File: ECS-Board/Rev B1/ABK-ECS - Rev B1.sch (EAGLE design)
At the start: 295 parts, among them J1 USB-B-S-RA, J10 22-05-7028-02, J11 RB1-125BAG1A, J12 22-05-7068-06, J13 22-05-7048-04, J14 22-05-7048-04, J15 22-05-7048-04, J2 MSTBA2, J3 22-05-7068-06, J4 22-05-7068-06, J5 22-05-7068-06, J6 22-05-7068-06, J7 22-05-7028-02, J8 FTSH-103-01-L-DV-NOPASTE, J9 FTSH-105-01-L-DV-NOPASTE, SW1 B3FS-1015, SW2 B3FS-1015, T1 MMBT2907ALT3, T10 MMBT2222AL, T11 IRLML5103TRPBF, T12 MMBT2222AL, T13 IRLML5103TRPBF, T14 IRLML5103TRPBF, T15 IRLML5103TRPBF, T16 IRLML5103TRPBF, T17 MMBT2222AL, T18 MMBT2222AL, T19 MMBT2222AL, T2 EXMACHINA-LOGO-NAME, T20 MMBT2222AL, T3 IRLML5103TRPBF, T4 IRLML5103TRPBF, T5 IRLML5103TRPBF, T6 IRLML5103TRPBF, T7 MMBT2222AL, T8 MMBT2222AL, T9 MMBT2222AL, U1 AT24C512C-SSHM-B, U2 LPC1768FBD100, U3 LT3686HDDPBF, U4 LT3686HDDPBF, U5 CD4050BD, U6 CD4050BD, U7 DP83848JSQ/NOPB, U8 SN74LVC2G17DBVR, U9 SN74LVC2G17DBVR, X1 FC-135, X2 ASE-12, X3 3000, X4 ASE_50

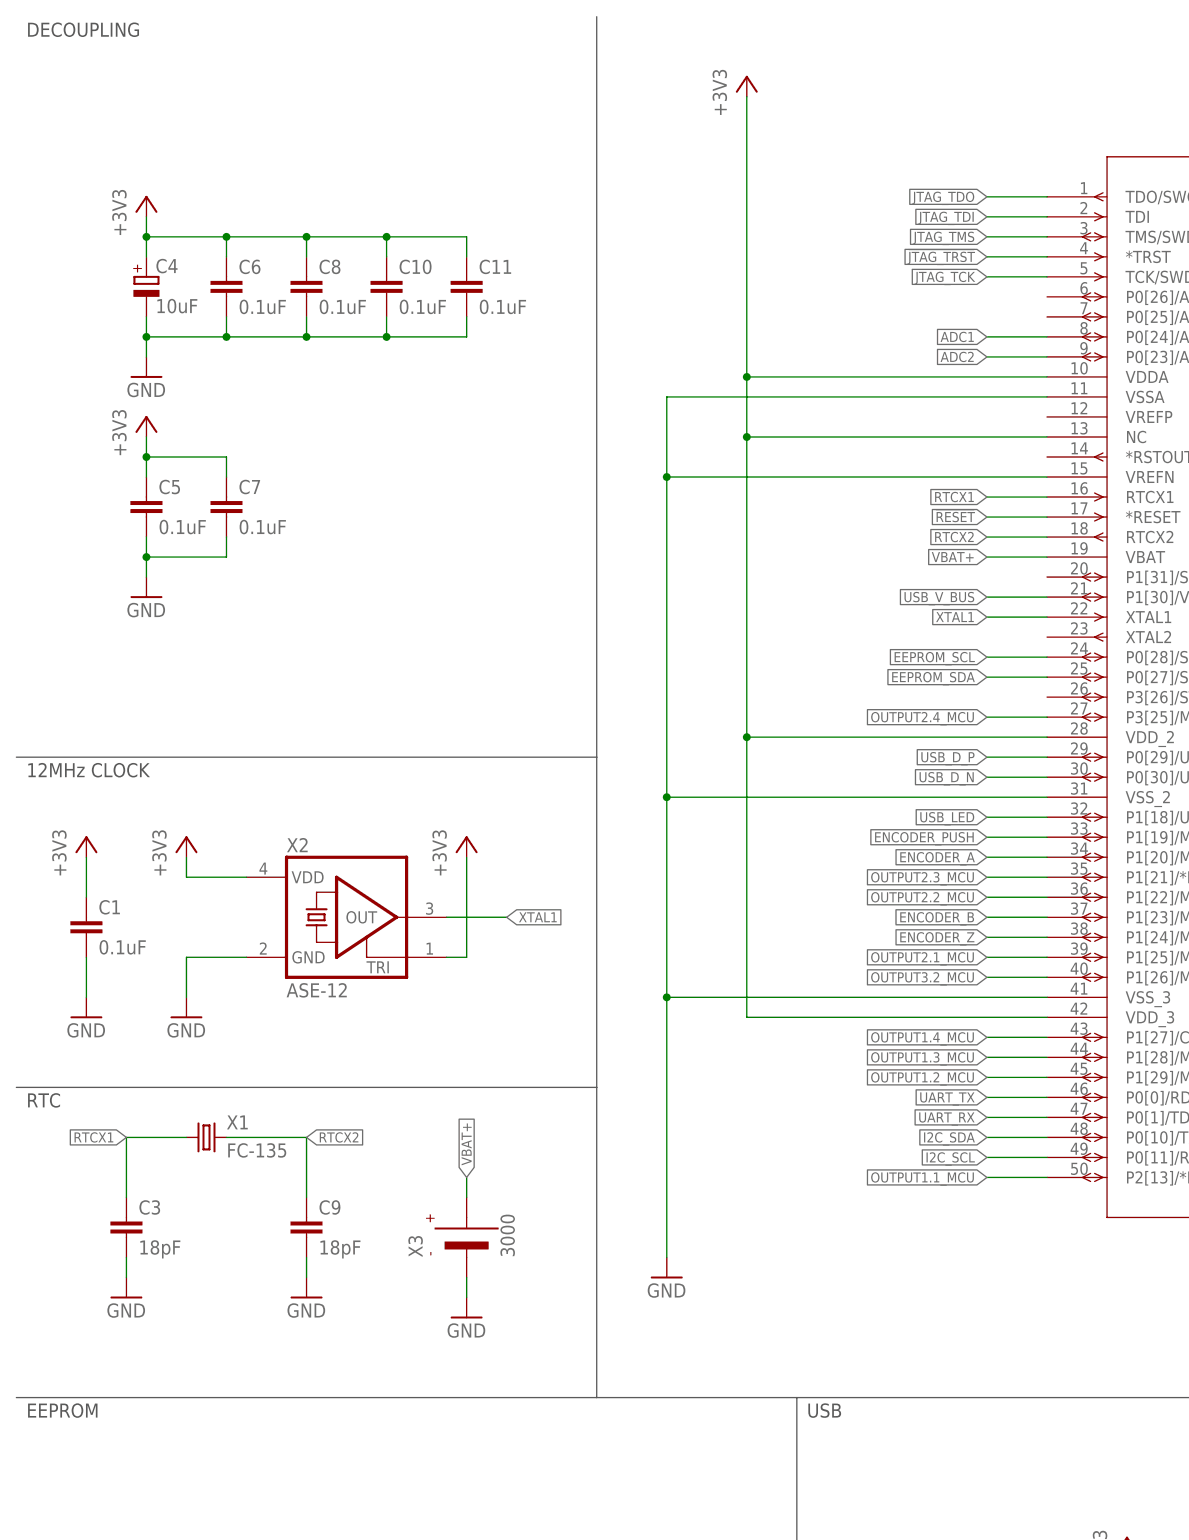
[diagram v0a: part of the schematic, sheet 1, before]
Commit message: Add and route decoupling power for VADC
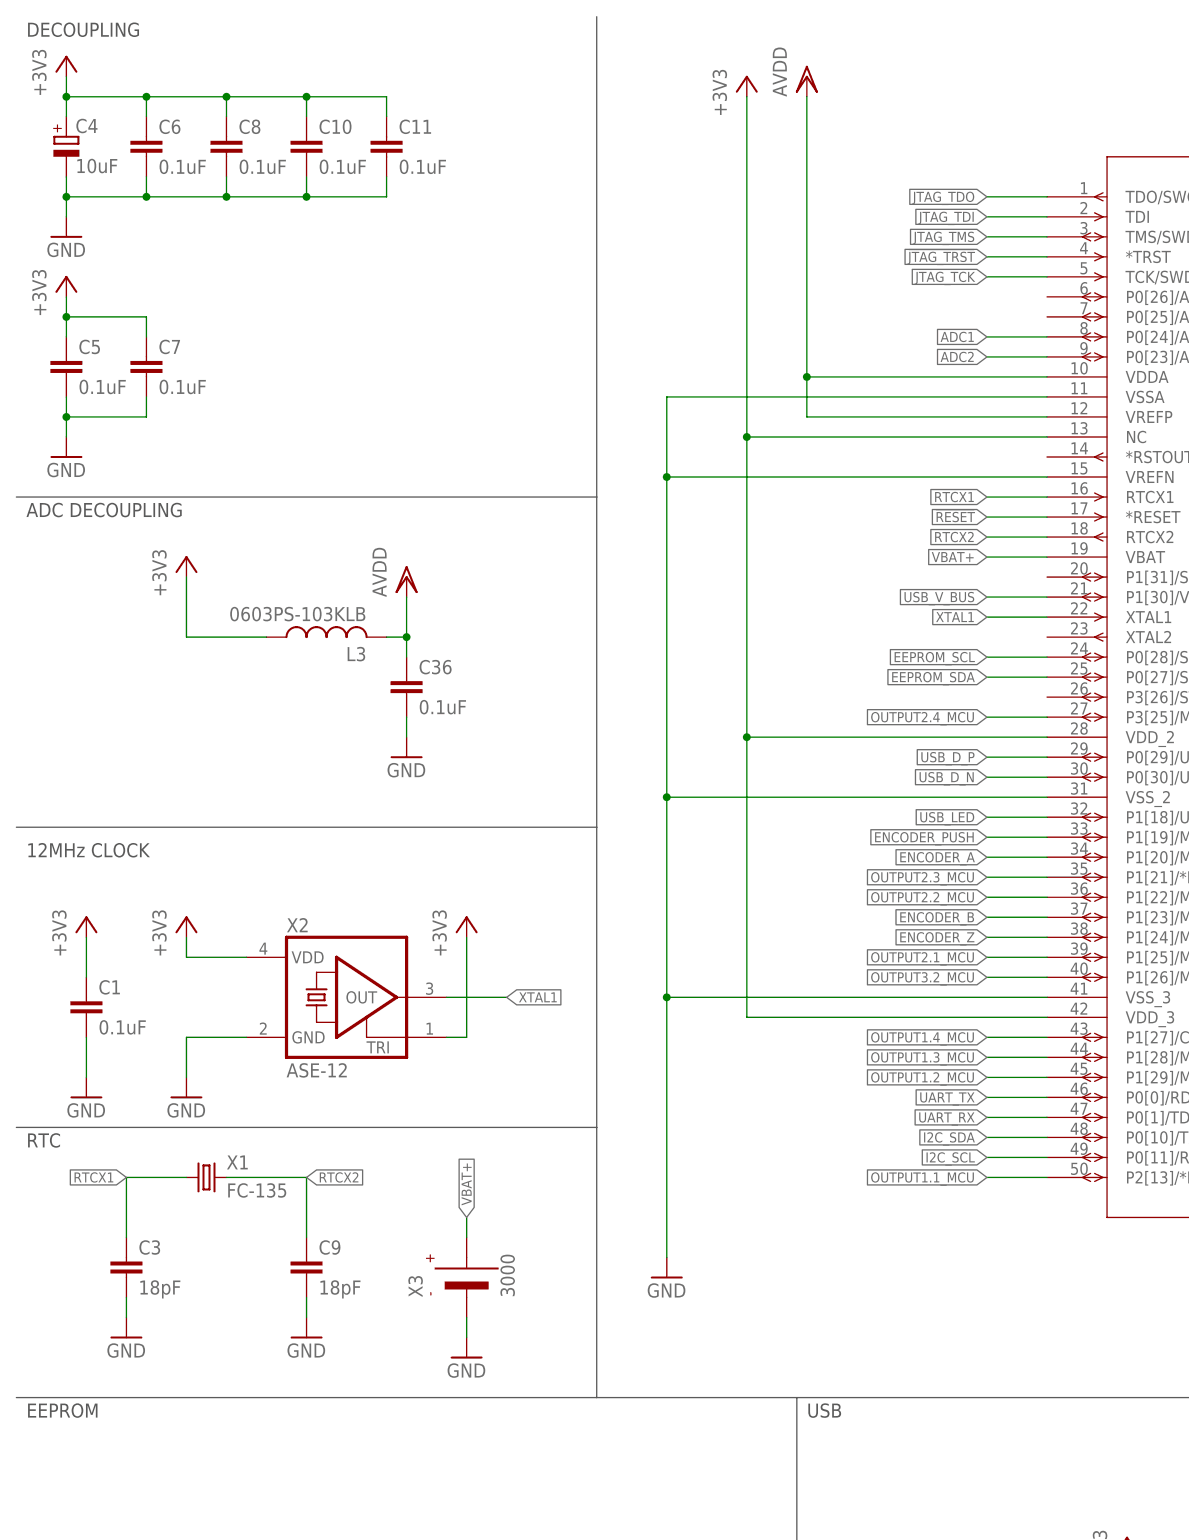
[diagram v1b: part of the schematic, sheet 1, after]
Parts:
- added C36: 0.1uF, rcl:C-EUC0603
- added L3: 0603PS-103KLB, coilcraft:0603PS
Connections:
- new net AVDD: C36.1, J13-1.S, L3.2, U2.VDDA, U2.VREFP
- net +3V3: now also L3.1; no longer U2.VDDA
- net GND: now also C36.2
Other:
- note added: "ADC DECOUPLING"
- moved on the sheet: C1, C10, C11, C3, C4, C5, C6, C7, C8, C9, X1, X2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

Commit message: Generated MDP files
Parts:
- removed R152: 1K, rcl:R-EU_R0603
- removed SJ6, SJ7: SJNC, SparkFun-Passives:SJNC
- added R6: 39K, rcl:R-EU_R0603
- added SJ1, SJ2: SJNC, SparkFun-Passives:SJNC
- C1: value 0.1uF -> 10uF; device rcl:C-EUC0603 -> rcl:CPOL-EUCT3216; MPN MC0603B104K160CT -> F931A106MAA; OC_NEWARK 06R4923 -> 58R3260
- C10, C5: value 0.1uF -> 18pF; MPN MC0603B104K160CT -> GRM1885C1H180JA01D; OC_NEWARK 06R4923 -> 14T3328
- C12: value 2.2uF -> 0.1uF; MPN GRT188R61H225KE13D -> MC0603B104K160CT; OC_NEWARK 01AC8938 -> 06R4923
- C14: value 1000pF -> 2.2uF; MPN GRM188R71H102KA01D -> GRT188R61H225KE13D; OC_NEWARK 19X1713 -> 01AC8938
- C16: value 2.2uF -> 1000pF; MPN GRT188R61H225KE13D -> GRM188R71H102KA01D; OC_NEWARK 01AC8938 -> 19X1713
- C18: value 22uF -> 2.2uF; device rcl:C-EUC0805 -> rcl:C-EUC0603; MF KEMET -> (none); MPN C0805C226M9PACTU -> GRT188R61H225KE13D; OC_NEWARK 70K9142 -> 01AC8938
- C20: value 0.1uF -> 22uF; device rcl:C-EUC0603 -> rcl:C-EUC0805; MF (none) -> KEMET; MPN MC0603B104K160CT -> C0805C226M9PACTU; OC_NEWARK 06R4923 -> 70K9142
- C22: value 4.7uF -> 0.1uF; device rcl:CPOL-EUCT3216 -> rcl:C-EUC0603; MPN F931A475MAA -> MC0603B104K160CT; OC_NEWARK 58R3271 -> 06R4923
- C23: value 100nF -> 4.7uF; device rcl:C-EUC0603 -> rcl:CPOL-EUCT3216; MPN MC0603B104K250CT -> F931A475MAA; OC_NEWARK 06R4925 -> 58R3271
- C25, C29: value 10uF -> 100nF; device rcl:CPOL-EUCT3216 -> rcl:C-EUC0603; MPN F931A106MAA -> MC0603B104K250CT; OC_NEWARK 58R3260 -> 06R4925
- C26, C30: value 100nF -> 10uF; device rcl:C-EUC0603 -> rcl:CPOL-EUCT3216; MPN MC0603B104K250CT -> F931A106MAA; OC_NEWARK 06R4925 -> 58R3260
- C3, C9: value 18pF -> 0.1uF; MPN GRM1885C1H180JA01D -> MC0603B104K160CT; OC_NEWARK 14T3328 -> 06R4923
- C34: value 0.1uF -> 100nF; MPN MC0603B104K160CT -> MC0603B104K250CT; OC_NEWARK 06R4923 -> 06R4925
- C4: value 10uF -> 0.1uF; device rcl:CPOL-EUCT3216 -> rcl:C-EUC0603; MPN F931A106MAA -> MC0603B104K160CT; OC_NEWARK 58R3260 -> 06R4923
- L1: value 15uH -> 0603PS-103KLB; device Wurth-POWER_MAGNETICS-rev16f:WE-PD2_5848/5820 -> coilcraft:0603PS; MPN 744774115 -> (none); OC_NEWARK 08P2818 -> unknown
- L2: value 10uH -> 15uH; MPN 74477410 -> 744774115; OC_NEWARK 08P2817 -> 08P2818
- L3: value 0603PS-103KLB -> 10uH; device coilcraft:0603PS -> Wurth-POWER_MAGNETICS-rev16f:WE-PD2_5848/5820; MPN (none) -> 74477410; OC_NEWARK unknown -> 08P2817
- R100, R69: value 10K -> 1K; MPN RC0603FR-0710KL -> RC0603FR-071KL; OC_NEWARK 68R0049 -> 68R0042
- R104, R73: value 1K -> 1K5; MPN RC0603FR-071KL -> RC0603FR-071K5L; OC_NEWARK 68R0042 -> 68R0045
- R108, R77: value 1K5 -> 4K7; MPN RC0603FR-071K5L -> RC0603FR-074K7L; OC_NEWARK 68R0045 -> 68R0092
- R11: value 33 -> 1K5; MPN RC0603FR-0733RL -> RC0603FR-071K5L; OC_NEWARK 68R0085 -> 68R0045
- R112, R81: value 4K7 -> 100; MPN RC0603FR-074K7L -> RC0603FR-13100RL; OC_NEWARK 68R0092 -> 68R0131
- R116, R85: value 100 -> 330; MPN RC0603FR-13100RL -> RC0603FR-07330RL; OC_NEWARK 68R0131 -> 98K7391
- R12: value 1K5 -> 10K; MPN RC0603FR-071K5L -> RC0603FR-0710KL; OC_NEWARK 68R0045 -> 68R0049
- R120: value 330 -> 0R; MPN RC0603FR-07330RL -> MCMR06X000 PTL; OC_NEWARK 98K7391 -> 86T3500
- R122: value 0R -> 220; MPN MCMR06X000 PTL -> MCMR06X2200FTL; OC_NEWARK 86T3500 -> 86T3577
- R124: value 220 -> 49.9; MPN MCMR06X2200FTL -> MCMR06X49R9FTL; OC_NEWARK 86T3577 -> 86T3659
- R128: value 49.9 -> 4K7; MPN MCMR06X49R9FTL -> MCMR06X4701FTL; OC_NEWARK 86T3659 -> 86T3649
- R129: value 4K7 -> 2K2; MPN MCMR06X4701FTL -> MCMR06X2201FTL; OC_NEWARK 86T3649 -> 86T3578
- R13: value 10K -> 0R; MPN RC0603FR-0710KL -> RC0603FR-070RL; OC_NEWARK 68R0049 -> 50Y7761
- R130: value 2K2 -> 1K; MPN MCMR06X2201FTL -> MCMR06X1001FTL; OC_NEWARK 86T3578 -> 86T3505
- R133, R138, R143: value 1K -> 4K7; MPN MCMR06X1001FTL -> MCMR06X2701FTL; OC_NEWARK 86T3505 -> 86T3598
- R135, R139, R144: value 4K7 -> 1K; MPN MCMR06X2701FTL -> MCMR06X1001FTL; OC_NEWARK 86T3598 -> 86T3505
- R15: value 0R -> 10K; MPN RC0603FR-070RL -> RC0603FR-0710KL; OC_NEWARK 50Y7761 -> 68R0049
- R16, R26: value 10K -> 1K5; MPN RC0603FR-0710KL -> RC0603FR-071K5L; OC_NEWARK 68R0049 -> 68R0045
- R18: value 1K5 -> 31K6; MPN RC0603FR-071K5L -> MCMR06X3162FTL; OC_FARNELL (none) -> 2073391; OC_NEWARK 68R0045 -> 86T3613
- R20: value 31K6 -> 4K7; MPN MCMR06X3162FTL -> RC0603FR-074K7L; OC_FARNELL 2073391 -> (none); OC_NEWARK 86T3613 -> 68R0092
- R22: value 4K7 -> 52K3; MPN RC0603FR-074K7L -> MC0063W0603152K3; OC_FARNELL (none) -> 2073391; OC_NEWARK 68R0092 -> 26M0962
- R23: value 52K3 -> 10K; MPN MC0063W0603152K3 -> RC0603FR-0710KL; OC_NEWARK 26M0962 -> 68R0049
- R24: value 10K -> 31K6; MPN RC0603FR-0710KL -> MCMR06X3162FTL; OC_NEWARK 68R0049 -> 86T3613
- R25: value 31K6 -> 10K; MPN MCMR06X3162FTL -> RC0603FR-0710KL; OC_NEWARK 86T3613 -> 68R0049
- R28: value 1K5 -> 1K; MPN RC0603FR-071K5L -> RC0603FR-071KL; OC_FARNELL 2073391 -> (none); OC_NEWARK 68R0045 -> 68R0042
- R36, R48: value 1K -> 4K7; MPN RC0603FR-071KL -> RC0603FR-074K7L; OC_NEWARK 68R0042 -> 68R0092
- R40: value 4K7 -> 1K; MPN RC0603FR-074K7L -> RC0603FR-071KL; OC_NEWARK 68R0092 -> 68R0042
- R52: value 4K7 -> 1K5; MPN RC0603FR-074K7L -> RC0603FR-071K5L; OC_NEWARK 68R0092 -> 68R0045
- R61: value 1K5 -> 1K; device rcl:R-EU_R0603 -> rcl:R-EU_R1206; MPN RC0603FR-071K5L -> (none); OC_NEWARK 68R0045 -> (none)
- R65, R90, R96: value 1K -> 10K; device rcl:R-EU_R1206 -> rcl:R-EU_R0603; MPN (none) -> RC0603FR-0710KL; OC_NEWARK (none) -> 68R0049
- R7: value 39K -> 24K
- R8: value 24K -> 0R, DNI; MPN (none) -> RC0603FR-070RL; OC_NEWARK (none) -> 50Y7761
- R89: value 330 -> 1K; device rcl:R-EU_R0603 -> rcl:R-EU_R1206; MPN RC0603FR-07330RL -> (none); OC_NEWARK 98K7391 -> (none)
- R9: value 0R, DNI -> 33; MPN RC0603FR-070RL -> RC0603FR-0733RL; OC_NEWARK 50Y7761 -> 68R0085
- R91: value 10K -> 100; MPN RC0603FR-0710KL -> RC0603FR-13100RL; OC_NEWARK 68R0049 -> 68R0131
- R92: value 100 -> 1K; device rcl:R-EU_R0603 -> rcl:R-EU_R1206; MPN RC0603FR-13100RL -> (none); OC_NEWARK 68R0131 -> (none)
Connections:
- net !ISP_BOOT: now also R120.2; no longer R121.2
- net !ISP_RST: now also R121.2; no longer R122.2
- net !RESET: now also R121.1, R15.1; no longer R122.1, R16.1
- net +24V: now also C14.1, R20.2, R65.2, R90.2, R96.2; no longer C12.1, R100.2, R22.2, R69.2, R91.2
- net +3V3: now also C1.+, C22.1, C23.+, C25.1, C3.1, C30.+, C36.1, C4.1, C9.1, L1.1, L3.2, R12.2, R122.2, R124.1, R129.1, R139.1, R141.1, R144.1, R146.1, R15.2, R24.2, R27.2, R8.1; no longer C1.1, C10.1, C19.1, C22.+, C23.1, C29.+, C30.1, C4.+, C5.1, L2.2, L3.1, R124.2, R128.1, R13.2, R130.1, R140.1, R142.1, R145.1, R147.1, R16.2, R25.2, R28.2, R9.1
- net +5V: now also C19.1, L2.2, R133.1, R138.1, R143.1, R22.2, R26.2; no longer C18.1, L1.2, R135.1, R139.1, R144.1, R23.2, R27.2
- net 1: now also SJ2.2; no longer SJ4.2
- net 2: now also SJ3.2; no longer SJ5.2
- net 3: now also SJ4.2; no longer SJ6.2
- net 4: now also SJ5.2; no longer SJ7.2
- net ADC1: now also R135.2; no longer R136.2
- net ADC2: now also R132.2; no longer R133.2
- net AVDD: now also C12.1, L1.2; no longer C36.1, L3.2
- net BOOT_SELECT_P2_10: now also R120.1, R13.1; no longer R121.1, R14.1
- net BOOT_SELECT_P2_12: now also R14.1; no longer R15.1
- net ETH_RX_N: now also R127.2; no longer R128.2
- net ETH_RX_P: now also R126.2; no longer R127.2
- net ETH_TX_N: now also R125.2; no longer R126.2
- net ETH_TX_P: now also R124.2; no longer R125.2
- net GND: now also C1.-, C16.2, C22.2, C23.-, C25.2, C26.-, C29.2, C30.-, C4.2, R104.2, R128.2, R140.1, R142.1, R145.1, R147.1, R16.2, R18.1, R23.1, R25.1, R36.2, R48.2, R6.1, R61.1, R73.2, R89.1, R92.1, SJ1.1, SJ2.1; no longer C1.2, C18.2, C22.-, C23.2, C25.-, C26.2, C29.-, C30.2, C4.-, R112.2, R129.2, R141.1, R143.1, R146.1, R148.1, R18.2, R20.1, R24.1, R26.1, R40.2, R61.2, R65.1, R7.1, R81.2, R90.1, R96.1, SJ6.1, SJ7.1
- net I2C_SCL: now also R130.2, R139.2; no longer R131.2, R141.2
- net I2C_SDA: now also R136.2, R144.2; no longer R137.2, R146.2
- net INPUT1.1: now also R47.2, R51.1; no longer R48.2, R52.1
- net INPUT1.2: now also R46.2, R50.1; no longer R47.2, R51.1
- net INPUT1.3: now also R45.2, R49.1; no longer R46.2, R50.1
- net INPUT1.4: now also R44.2, R48.1; no longer R45.2, R49.1
- net INPUT2.1: now also R35.2, R39.1; no longer R36.2, R40.1
- net INPUT2.2: now also R34.2, R38.1; no longer R35.2, R39.1
- net INPUT2.3: now also R33.2, R37.1; no longer R34.2, R38.1
- net INPUT2.4: now also R32.2, R36.1; no longer R33.2, R37.1
- net MII_MODE: now also R129.2; no longer R130.2
- net MOTOR_VFQ: now also R89.2; no longer R90.2
- net N$1: now also R10.1, R11.2; no longer R11.1, R12.2
- net N$10: now also C17.1; no longer C16.1
- net N$100: now also R44.1; no longer R45.1
- net N$101: now also R41.2; no longer R42.2
- net N$102: now also R41.1; no longer R42.1
- net N$103: now also R45.1; no longer R46.1
- net N$104: now also R42.2; no longer R43.2
- net N$105: now also R42.1; no longer R43.1
- net N$106: now also R46.1; no longer R47.1
- net N$107: now also R57.1; no longer R58.1
- net N$108: now also R58.1; no longer R59.1
- net N$109: now also R59.1; no longer R60.1
- net N$11: now also C17.2, L2.1; no longer C16.2, L1.1
- net N$110: now also R47.1; no longer R48.1
- net N$111: now also R43.2; no longer R44.2
- net N$112: now also R43.1; no longer R44.1
- net N$113: now also R122.1; no longer R123.1
- net N$114: now also R7.2; no longer R8.2
- net N$115: now also R123.1; no longer R124.1
- net N$116: now also R128.1; no longer R129.1
- net N$117: now also R133.2, R150.1; no longer R134.2, R151.1
- net N$118: now also R134.2, R148.1; no longer R135.2, R149.1
- net N$119: now also R138.2, R151.1; no longer R139.2, R152.1
- net N$120: now also R149.2; no longer R150.2
- net N$121: now also R148.2; no longer R149.2
- net N$122: now also R150.2; no longer R151.2
- net N$123: now also R151.2; no longer R152.2
- net N$124: now also R143.2, R149.1; no longer R144.2, R150.1
- net N$125: now also R132.1; no longer R133.1
- net N$126: now also R135.1; no longer R136.1
- net N$127: now also R130.1; no longer R131.1
- net N$128: now also R136.1; no longer R137.1
- net N$129: now also R131.1; no longer R132.1
- net N$13: now also R24.1, R25.2; no longer R25.1, R26.2
- net N$130: now also R137.1; no longer R138.1
- net N$14: now also C18.1; no longer C17.1
- net N$15: now also C18.2, L3.1; no longer C17.2, L2.1
- net N$17: now also R100.2; no longer R101.2
- net N$18: now also R96.1; no longer R97.1
- net N$19: now also R101.2; no longer R102.2
- net N$2: now also R9.1; no longer R10.1
- net N$20: now also R97.1; no longer R98.1
- net N$21: now also R102.2; no longer R103.2
- net N$22: now also R98.1; no longer R99.1
- net N$23: now also R103.2; no longer R104.2
- net N$24: now also R99.1; no longer R100.1
- net N$25: now also R91.1; no longer R92.1
- net N$26: now also R90.1; no longer R91.1
- net N$29: now also R16.1; no longer R17.1
- net N$3: now also R17.1; no longer R18.1
- net N$30: now also R11.1, R8.2; no longer R12.1, R9.2
- net N$31: now also R69.1, R77.1, R81.1; no longer R70.1, R78.1, R82.1
- net N$33: now also R81.2; no longer R82.2
- net N$34: now also R70.1, R78.1, R82.1; no longer R71.1, R79.1, R83.1
- net N$35: now also R82.2; no longer R83.2
- net N$36: now also R71.1, R79.1, R83.1; no longer R72.1, R80.1, R84.1
- net N$37: now also R72.1, R80.1, R84.1; no longer R73.1, R81.1, R85.1
- net N$38: now also R83.2; no longer R84.2
- net N$39: now also R84.2; no longer R85.2
- net N$4: now also R18.2; no longer R19.2
- net N$40: now also R85.1; no longer R86.1
- net N$41: now also R28.2; no longer R29.2
- net N$42: now also R86.1; no longer R87.1
- net N$43: now also R88.1; no longer R89.1
- net N$44: now also R21.1; no longer R22.1
- net N$45: now also R20.1; no longer R21.1
- net N$46: now also R87.1; no longer R88.1
- net N$47: now also R29.2; no longer R30.2
- net N$48: now also R30.2; no longer R31.2
- net N$49: now also R31.2; no longer R32.2
- net N$5: now also R12.1, R13.2; no longer R13.1, R15.2
- net N$50: now also R27.1; no longer R28.1
- net N$51: now also R26.1; no longer R27.1
- net N$52: now also R31.1; no longer R32.1
- net N$53: now also R30.1; no longer R31.1
- net N$54: now also R29.1; no longer R30.1
- net N$55: now also R28.1; no longer R29.1
- net N$56: now also R52.1; no longer R53.1
- net N$57: now also R53.1; no longer R54.1
- net N$58: now also R54.1; no longer R55.1
- net N$59: now also R55.1; no longer R56.1
- net N$6: now also C15.1; no longer C14.1
- net N$61: now also R35.1; no longer R36.1
- net N$62: now also R34.1; no longer R35.1
- net N$63: now also R33.1; no longer R34.1
- net N$64: now also R32.1; no longer R33.1
- net N$65: now also R56.1; no longer R57.1
- net N$66: now also R73.1; no longer R74.1
- net N$67: now also R74.1; no longer R75.1
- net N$68: now also R75.1; no longer R76.1
- net N$69: now also R76.1; no longer R77.1
- net N$7: now also R19.2; no longer R20.2
- net N$70: now also SJ1.2; no longer SJ3.2
- net N$71: now also R65.1; no longer R66.1
- net N$72: now also R66.1; no longer R67.1
- net N$75: now also R100.1, R108.1, R112.1; no longer R101.1, R109.1, R113.1
- net N$76: now also R112.2; no longer R113.2
- net N$77: now also R67.1; no longer R68.1
- net N$78: now also R68.1; no longer R69.1
- net N$79: now also R101.1, R109.1, R113.1; no longer R102.1, R110.1, R114.1
- net N$8: now also C16.1; no longer C15.1
- net N$80: now also R113.2; no longer R114.2
- net N$81: now also R40.2; no longer R41.2
- net N$82: now also R40.1; no longer R41.1
- net N$83: now also R102.1, R110.1, R114.1; no longer R103.1, R111.1, R115.1
- net N$84: now also R69.2; no longer R70.2
- net N$85: now also R70.2; no longer R71.2
- net N$86: now also R103.1, R111.1, R115.1; no longer R104.1, R112.1, R116.1
- net N$87: now also R114.2; no longer R115.2
- net N$88: now also R115.2; no longer R116.2
- net N$89: now also R116.1; no longer R117.1
- net N$9: now also R22.1, R23.2; no longer R23.1, R24.2
- net N$90: now also R60.1; no longer R61.1
- net N$91: now also R117.1; no longer R118.1
- net N$92: now also R119.1; no longer R120.1
- net N$93: now also R118.1; no longer R119.1
- net N$94: now also R104.1; no longer R105.1
- net N$95: now also R105.1; no longer R106.1
- net N$96: now also R106.1; no longer R107.1
- net N$97: now also R107.1; no longer R108.1
- net N$98: now also R71.2; no longer R72.2
- net N$99: now also R72.2; no longer R73.2
- net OUTPUT1.1: now also R61.2; no longer R62.2
- net OUTPUT1.1_MCU: now also R85.2; no longer R86.2
- net OUTPUT1.2: now also R62.2; no longer R63.2
- net OUTPUT1.2_MCU: now also R86.2; no longer R87.2
- net OUTPUT1.3: now also R63.2; no longer R64.2
- net OUTPUT1.3_MCU: now also R87.2; no longer R88.2
- net OUTPUT1.4: now also R64.2; no longer R65.2
- net OUTPUT1.4_MCU: now also R88.2; no longer R89.2
- net OUTPUT2.1: now also R92.2; no longer R93.2
- net OUTPUT2.1_MCU: now also R116.2; no longer R117.2
- net OUTPUT2.2: now also R93.2; no longer R94.2
- net OUTPUT2.2_MCU: now also R117.2; no longer R118.2
- net OUTPUT2.3: now also R94.2; no longer R95.2
- net OUTPUT2.3_MCU: now also R118.2; no longer R119.2
- net OUTPUT2.4: now also R95.2; no longer R96.2
- net OUTPUT2.4_MCU: now also R119.2; no longer R120.2
- net OUTPUT3.2_MCU: now also R91.2; no longer R92.2
- net PFBOUT: now also C26.+, C29.1; no longer C25.+, C26.1
- net RTCX1: now also C5.1; no longer C3.1
- net RTCX2: now also C10.1; no longer C9.1
- net UART_RX: now also R131.2, R141.2; no longer R132.2, R143.2
- net UART_TX: now also R137.2, R146.2; no longer R138.2, R148.2
- net USB_D_N: now also R9.2; no longer R10.2
- net USB_D_P: now also R10.2; no longer R11.2
- net USB_V_BUS: now also R6.2, R7.1; no longer R7.2, R8.1
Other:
- moved on the sheet: C10, C13, C14, C15, C16, C17, C18, C19, C2, C21, C24, C27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
